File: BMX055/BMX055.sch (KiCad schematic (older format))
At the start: 26 parts, among them J1 Conn_01x06, J2 Conn_01x04, J3 Conn_01x06, J4 Conn_01x04, Q2 BSS138DW, U1 AP2127K-3.3, U2 BMX055

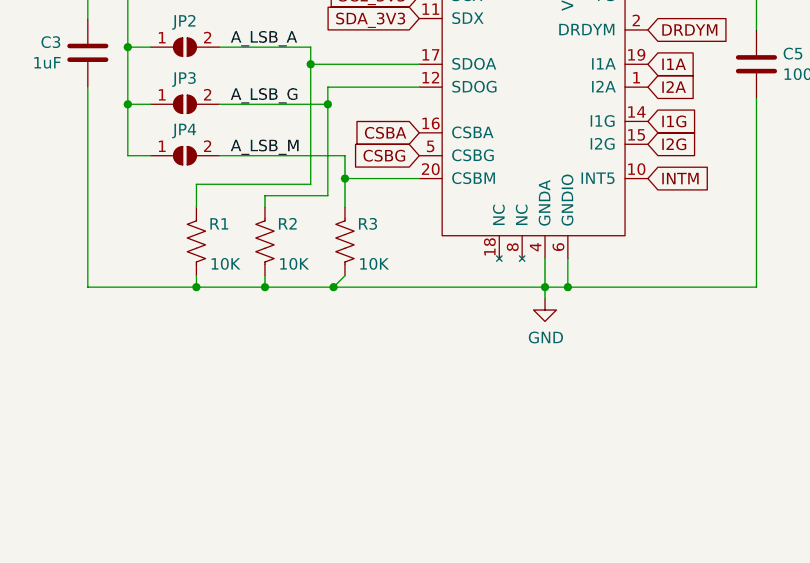
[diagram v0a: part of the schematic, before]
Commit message: Schematic and 3D render updates
Multiple boards
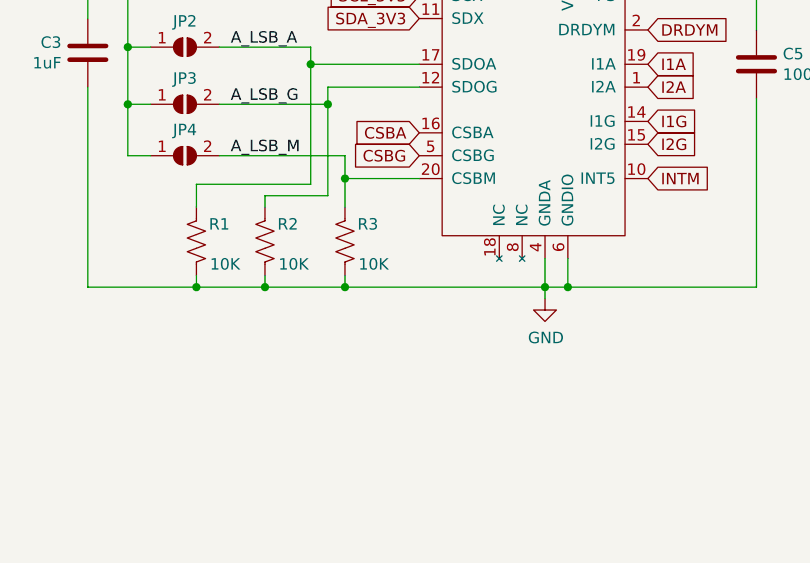
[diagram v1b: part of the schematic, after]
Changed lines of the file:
@@
 $EndComp
-Wire Wire Line
-	4675 3800 4625 3850
-Wire Wire Line
-	4625 3850 5550 3850
-Wire Wire Line
-	4625 3850 4325 3850
-Connection ~ 4625 3850
 Wire Wire Line
 	4325 3850 4025 3850
@@
 Connection ~ 4600 3050
 Connection ~ 4525 2875
+Wire Wire Line
+	4675 3800 4675 3850
+Wire Wire Line
+	4675 3850 5550 3850
+Wire Wire Line
+	4675 3850 4325 3850
+Connection ~ 4675 3850
 $EndSCHEMATC
